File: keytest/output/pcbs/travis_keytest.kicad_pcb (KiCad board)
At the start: 2 copper layers, 42.4 x 59.7 mm, 8 parts

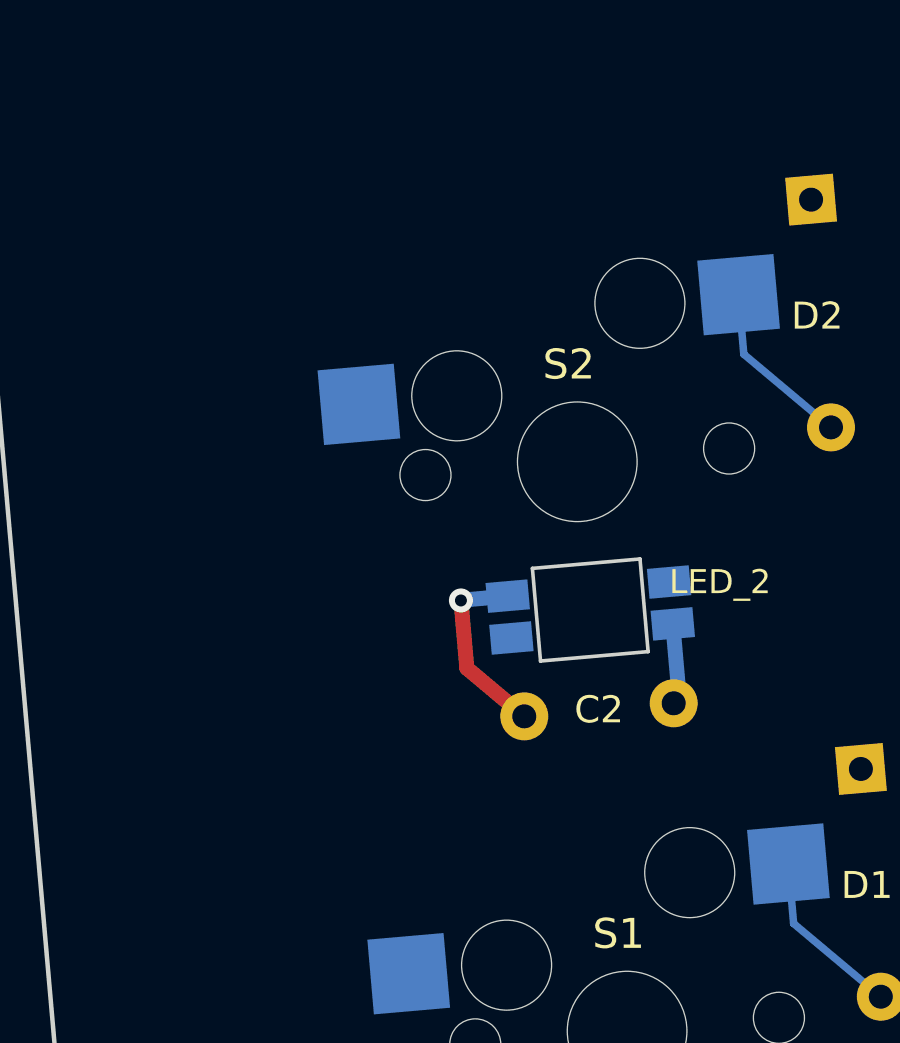
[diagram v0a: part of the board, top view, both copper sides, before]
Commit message: footprint updates
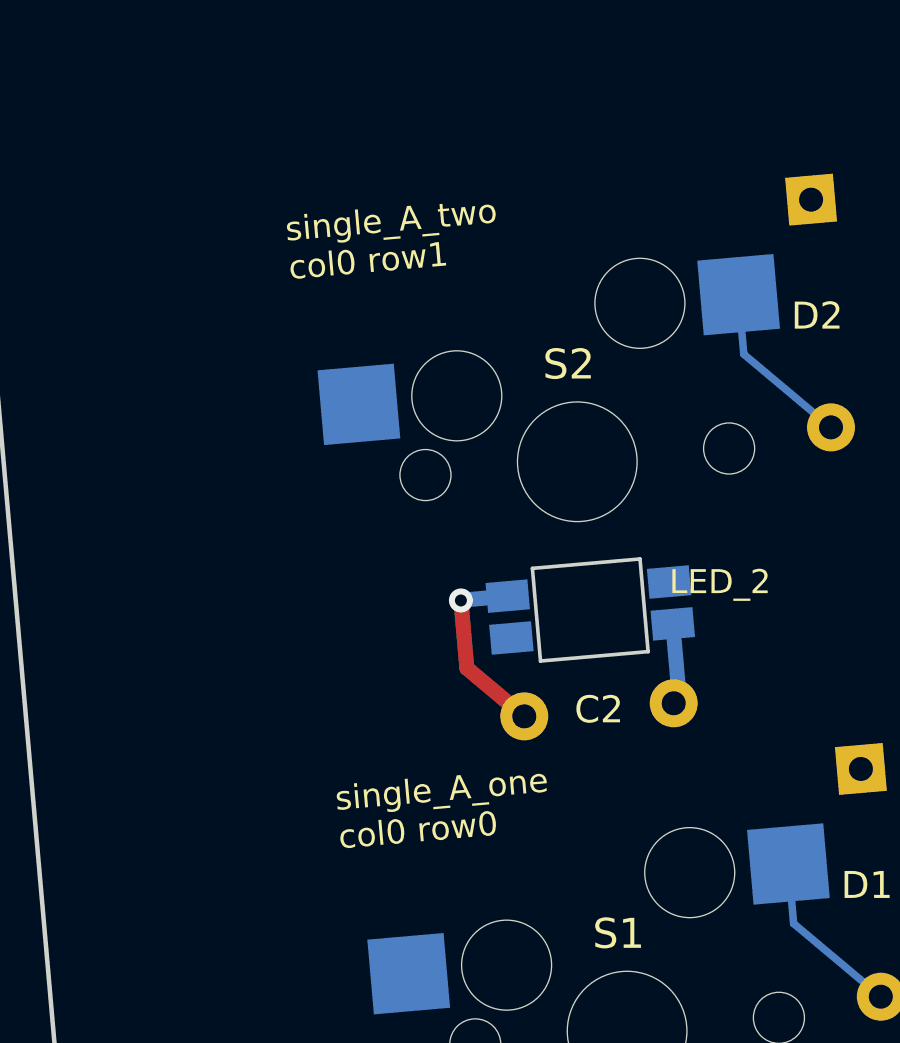
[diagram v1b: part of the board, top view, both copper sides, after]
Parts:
- C1, C2: footprint C_Disc_D4.7mm_W2.5mm_P5.00mm -> travis:C_Disc_D4.7mm_W2.5mm_P5.00mm
- D1, D2: footprint Diode_DO-35 -> travis:Diode_DO-35
- LED1, LED2: footprint ceoloide:led_SK6812mini-e (per-key single-side) -> travis:led_SK6812mini-e (per-key single-side)
- S1, S2: footprint MX -> travis:MX
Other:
- board text added: "single_A_one col0 row0"
- board text added: "single_A_two col0 row1"
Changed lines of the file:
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@@
 (add_net "LED_3")
   )
-(module MX (layer F.Cu)
+(module "travis:MX" (layer F.Cu)
     (at 100 100 5)
     (fp_text reference "S1" (at 0 -3.25) (layer F.SilkS)  (effects (font (size 1 1) (thickness 0.15))))
@@
     )
 )
-(module "Diode_DO-35" (layer "B.Cu")
+(gr_text "single_A_one\ncol0 row0" (at 90.2228 91.7959 5) (layer F.SilkS)
+  (effects (font (size 0.8 0.8) (thickness 0.15)) (justify top left))
+)
+(gr_text "single_A_one\ncol0 row0" (at 90.2228 91.7959  5) (layer B.SilkS)
+  (effects (font (size 0.8 0.8) (thickness 0.15)) (justify top right mirror))
+)
+(module "travis:Diode_DO-35" (layer "B.Cu")
   (descr "Diode, DO-35_SOD27 series, Axial, Horizontal, pin pitch=7.62mm, , length*diameter=4*2mm^2, , http://www.diodes.com/_files/packages/DO-35.pdf")
   (tags "Diode DO-35_SOD27 series Axial Horizontal pin pitch 7.62mm  length 4mm diameter 2mm")
@@
   (effects (font (size 0.9 0.9) (thickness 0.15)) (justify left))
 )
-(module "ceoloide:led_SK6812mini-e (per-key single-side)"
+(module "travis:led_SK6812mini-e (per-key single-side)"
   (layer B.Cu)
   (at 100.4323 104.9411 5)
@@
   (effects (font (size 0.8 0.8) (thickness 0.15)) (justify right))
 )
-(module C_Disc_D4.7mm_W2.5mm_P5.00mm (layer B.Cu)
+(module "travis:C_Disc_D4.7mm_W2.5mm_P5.00mm" (layer B.Cu)
   (descr "C, Disc series, Radial, pin pitch=5.00mm, , diameter*width=4.7*2.5mm^2, Capacitor, http://www.vishay.com/docs/45233/krseries.pdf")
   (tags "C Disc series Radial pin pitch 5.00mm  diameter 4.7mm width 2.5mm Capacitor")
@@
   (net 7)
 )
-(module MX (layer F.Cu)
+(module "travis:MX" (layer F.Cu)
     (at 98.3396831 81.022491 5)
     (fp_text reference "S2" (at 0 -3.25) (layer F.SilkS)  (effects (font (size 1 1) (thickness 0.15))))
@@
     )
 )
-(module "Diode_DO-35" (layer "B.Cu")
+(gr_text "single_A_two\ncol0 row1" (at 88.5624 72.8184 5) (layer F.SilkS)
+  (effects (font (size 0.8 0.8) (thickness 0.15)) (justify top left))
+)
+(gr_text "single_A_two\ncol0 row1" (at 88.5624 72.8184  5) (layer B.SilkS)
+  (effects (font (size 0.8 0.8) (thickness 0.15)) (justify top right mirror))
+)
+(module "travis:Diode_DO-35" (layer "B.Cu")
   (descr "Diode, DO-35_SOD27 series, Axial, Horizontal, pin pitch=7.62mm, , length*diameter=4*2mm^2, , http://www.diodes.com/_files/packages/DO-35.pdf")
   (tags "Diode DO-35_SOD27 series Axial Horizontal pin pitch 7.62mm  length 4mm diameter 2mm")
@@
   (effects (font (size 0.9 0.9) (thickness 0.15)) (justify left))
 )
-(module "ceoloide:led_SK6812mini-e (per-key single-side)"
+(module "travis:led_SK6812mini-e (per-key single-side)"
   (layer B.Cu)
   (at 98.7720 85.9636 185)
@@
   (effects (font (size 0.8 0.8) (thickness 0.15)) (justify left))
 )
-(module C_Disc_D4.7mm_W2.5mm_P5.00mm (layer B.Cu)
+(module "travis:C_Disc_D4.7mm_W2.5mm_P5.00mm" (layer B.Cu)
   (descr "C, Disc series, Radial, pin pitch=5.00mm, , diameter*width=4.7*2.5mm^2, Capacitor, http://www.vishay.com/docs/45233/krseries.pdf")
   (tags "C Disc series Radial pin pitch 5.00mm  diameter 4.7mm width 2.5mm Capacitor")

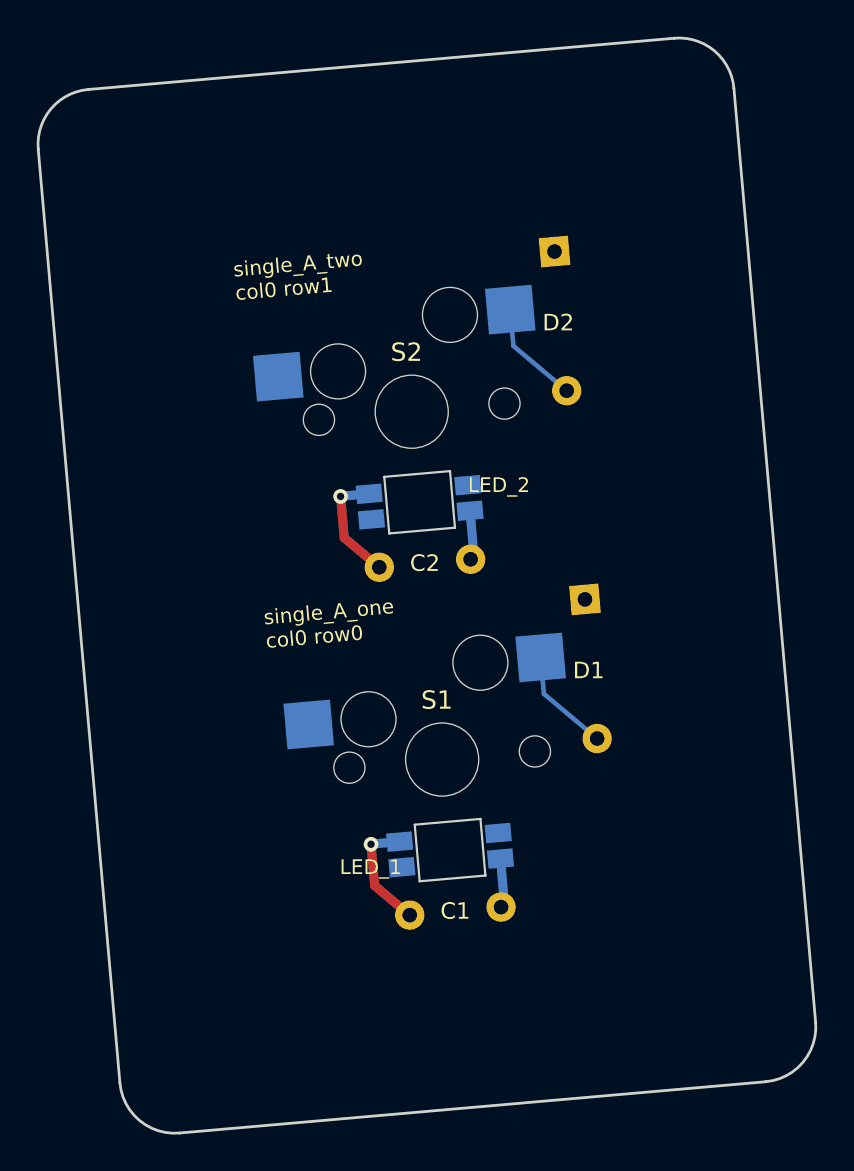
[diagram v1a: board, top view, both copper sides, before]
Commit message: minor label fix
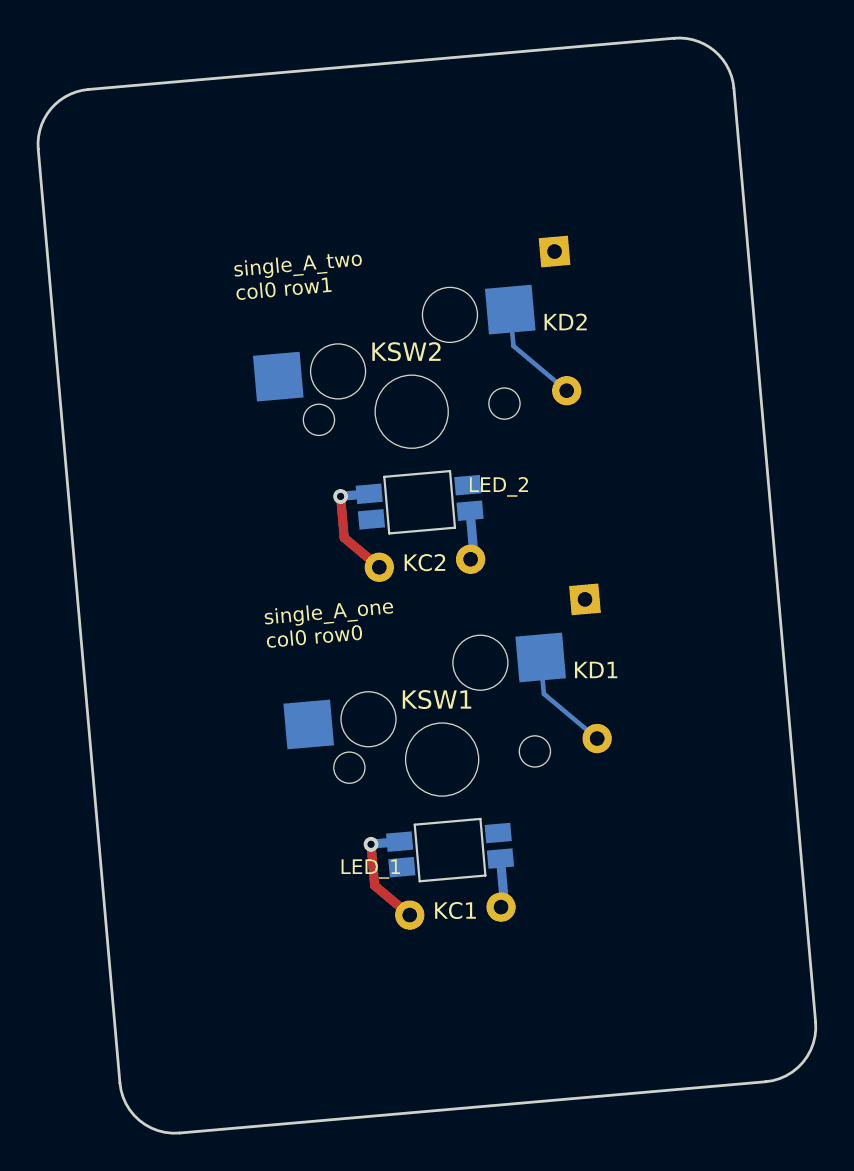
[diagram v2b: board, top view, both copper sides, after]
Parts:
- removed C1, C2: 104, travis:C_Disc_D4.7mm_W2.5mm_P5.00mm
- removed D1, D2: 1N4148, travis:Diode_DO-35
- removed LED1, LED2: SK6812mini-e, travis:led_SK6812mini-e (per-key single-side)
- removed S1, S2: Kailh MX Switch Sockets, travis:MX
- added KC1: 104, travis:C_Disc_D4.7mm_W2.5mm_P5.00mm, B.Cu at (103.2, 108.1)
- added KC2: 104, travis:C_Disc_D4.7mm_W2.5mm_P5.00mm, B.Cu at (96.6, 89.5)
- added KD1: 1N4148, travis:Diode_DO-35, B.Cu at (107.8, 91.3)
- added KD2: 1N4148, travis:Diode_DO-35, B.Cu at (106.1, 72.3)
- added KLED1: SK6812mini-e, travis:led_SK6812mini-e (per-key single-side), B.Cu at (100.4, 104.9)
- added KLED2: SK6812mini-e, travis:led_SK6812mini-e (per-key single-side), B.Cu at (98.8, 86.0)
- added KSW1: Kailh MX Switch Sockets, travis:MX, F.Cu at (100.0, 100.0)
- added KSW2: Kailh MX Switch Sockets, travis:MX, F.Cu at (98.3, 81.0)
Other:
- board text added: "KC1"
- board text added: "KC2"
- board text added: "KD1"
- board text added: "KD2"
- board text removed: "C1"
- board text removed: "C2"
- board text removed: "D1"
- board text removed: "D2"
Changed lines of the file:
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@@
 (module "travis:MX" (layer F.Cu)
     (at 100 100 5)
-    (fp_text reference "S1" (at 0 -3.25) (layer F.SilkS)  (effects (font (size 1 1) (thickness 0.15))))
+    (fp_text reference "KSW1" (at 0 -3.25) (layer F.SilkS)  (effects (font (size 1 1) (thickness 0.15))))
     (fp_text value "Kailh MX Switch Sockets" (at 0 0) (layer B.Fab) hide (effects (font (size 1 1) (thickness 0.15))))
     (fp_line (start -7 -6) (end -7 -7) (layer Dwgs.User) (width 0.15))
@@
   (tags "Diode DO-35_SOD27 series Axial Horizontal pin pitch 7.62mm  length 4mm diameter 2mm")
   (at 107.7931 91.2625 275)
-  (fp_text reference "D1" (at 5.985 1.921 275) (layer "B.SilkS")
+  (fp_text reference "KD1" (at 5.985 1.921 275) (layer "B.SilkS")
     (effects (font (size 1 1) (thickness 0.15)) (justify mirror))
   )
@@
   )
 )
-(gr_text "D1" (at 107.1290 95.1452 0) (layer F.SilkS)
+(gr_text "KD1" (at 107.1290 95.1452 0) (layer F.SilkS)
   (effects (font (size 0.9 0.9) (thickness 0.15)) (justify left))
 )
@@
   (layer B.Cu)
   (at 100.4323 104.9411 5)
-  (fp_text reference "LED1" (at -5.25 0 95) (layer B.SilkS)
+  (fp_text reference "KLED1" (at -5.25 0 95) (layer B.SilkS)
     (effects (font (size 1 1) (thickness 0.15)) (justify mirror))
   )
@@
   (tags "C Disc series Radial pin pitch 5.00mm  diameter 4.7mm width 2.5mm Capacitor")
   (at 103.2139 108.0505 185)
-  (fp_text reference "C1" (at 6.0 0 185) (layer B.SilkS)
+  (fp_text reference "KC1" (at 6.0 0 185) (layer B.SilkS)
     (effects (font (size 1 1) (thickness 0.15)) (justify left mirror))
   )
@@
   )
 )
-(gr_text "C1" (at 100.7234 108.2684 0) (layer F.SilkS)
+(gr_text "KC1" (at 100.7234 108.2684 0) (layer F.SilkS)
   (effects (font (size 0.9 0.9) (thickness 0.15)))
 )
@@
 (module "travis:MX" (layer F.Cu)
     (at 98.3396831 81.022491 5)
-    (fp_text reference "S2" (at 0 -3.25) (layer F.SilkS)  (effects (font (size 1 1) (thickness 0.15))))
+    (fp_text reference "KSW2" (at 0 -3.25) (layer F.SilkS)  (effects (font (size 1 1) (thickness 0.15))))
     (fp_text value "Kailh MX Switch Sockets" (at 0 0) (layer B.Fab) hide (effects (font (size 1 1) (thickness 0.15))))
     (fp_line (start -7 -6) (end -7 -7) (layer Dwgs.User) (width 0.15))
@@
   (tags "Diode DO-35_SOD27 series Axial Horizontal pin pitch 7.62mm  length 4mm diameter 2mm")
   (at 106.1328 72.2850 275)
-  (fp_text reference "D2" (at 5.985 1.921 275) (layer "B.SilkS")
+  (fp_text reference "KD2" (at 5.985 1.921 275) (layer "B.SilkS")
     (effects (font (size 1 1) (thickness 0.15)) (justify mirror))
   )
@@
   )
 )
-(gr_text "D2" (at 105.4687 76.1677 0) (layer F.SilkS)
+(gr_text "KD2" (at 105.4687 76.1677 0) (layer F.SilkS)
   (effects (font (size 0.9 0.9) (thickness 0.15)) (justify left))
 )
@@
   (layer B.Cu)
   (at 98.7720 85.9636 185)
-  (fp_text reference "LED2" (at -4.75 0 95) (layer B.SilkS)
+  (fp_text reference "KLED2" (at -4.75 0 95) (layer B.SilkS)
     (effects (font (size 1 1) (thickness 0.15)) (justify mirror))
   )
@@
   (tags "C Disc series Radial pin pitch 5.00mm  diameter 4.7mm width 2.5mm Capacitor")
   (at 96.5726 89.5088 5)
-  (fp_text reference "C2" (at 6.0 0 5) (layer B.SilkS)
+  (fp_text reference "KC2" (at 6.0 0 5) (layer B.SilkS)
     (effects (font (size 1 1) (thickness 0.15)) (justify right mirror))
   )
@@
   )
 )
-(gr_text "C2" (at 99.0631 89.2909 0) (layer F.SilkS)
+(gr_text "KC2" (at 99.0631 89.2909 0) (layer F.SilkS)
   (effects (font (size 0.9 0.9) (thickness 0.15)))
 )

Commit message: footprint/module updates
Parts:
- KC1, KC2: footprint travis:C_Disc_D4.7mm_W2.5mm_P5.00mm -> Capacitor_THT:C_Disc_D4.7mm_W2.5mm_P5.00mm
- KD1, KD2: footprint travis:Diode_DO-35 -> ScottoKeebs_Components:Diode_DO-35
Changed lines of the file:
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@@
   (effects (font (size 0.8 0.8) (thickness 0.15)) (justify top right mirror))
 )
-(module "travis:Diode_DO-35" (layer "B.Cu")
+(module "ScottoKeebs_Components:Diode_DO-35" (layer "B.Cu")
   (descr "Diode, DO-35_SOD27 series, Axial, Horizontal, pin pitch=7.62mm, , length*diameter=4*2mm^2, , http://www.diodes.com/_files/packages/DO-35.pdf")
   (tags "Diode DO-35_SOD27 series Axial Horizontal pin pitch 7.62mm  length 4mm diameter 2mm")
@@
   (effects (font (size 0.8 0.8) (thickness 0.15)) (justify right))
 )
-(module "travis:C_Disc_D4.7mm_W2.5mm_P5.00mm" (layer B.Cu)
+(module "Capacitor_THT:C_Disc_D4.7mm_W2.5mm_P5.00mm" (layer B.Cu)
   (descr "C, Disc series, Radial, pin pitch=5.00mm, , diameter*width=4.7*2.5mm^2, Capacitor, http://www.vishay.com/docs/45233/krseries.pdf")
   (tags "C Disc series Radial pin pitch 5.00mm  diameter 4.7mm width 2.5mm Capacitor")
@@
   (effects (font (size 0.8 0.8) (thickness 0.15)) (justify top right mirror))
 )
-(module "travis:Diode_DO-35" (layer "B.Cu")
+(module "ScottoKeebs_Components:Diode_DO-35" (layer "B.Cu")
   (descr "Diode, DO-35_SOD27 series, Axial, Horizontal, pin pitch=7.62mm, , length*diameter=4*2mm^2, , http://www.diodes.com/_files/packages/DO-35.pdf")
   (tags "Diode DO-35_SOD27 series Axial Horizontal pin pitch 7.62mm  length 4mm diameter 2mm")
@@
   (effects (font (size 0.8 0.8) (thickness 0.15)) (justify left))
 )
-(module "travis:C_Disc_D4.7mm_W2.5mm_P5.00mm" (layer B.Cu)
+(module "Capacitor_THT:C_Disc_D4.7mm_W2.5mm_P5.00mm" (layer B.Cu)
   (descr "C, Disc series, Radial, pin pitch=5.00mm, , diameter*width=4.7*2.5mm^2, Capacitor, http://www.vishay.com/docs/45233/krseries.pdf")
   (tags "C Disc series Radial pin pitch 5.00mm  diameter 4.7mm width 2.5mm Capacitor")
